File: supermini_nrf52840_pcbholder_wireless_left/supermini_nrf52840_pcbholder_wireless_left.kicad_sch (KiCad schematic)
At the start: 9 parts, among them J1 Conn_01x07_Pin, J2 Conn_01x02_Pin, J3 Conn_01x07_Pin, J4 Conn_01x04_Pin, SW1 SW_SPDT, SW2 SW_SPST, U1 nice_nano

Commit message: create left side and tweaks
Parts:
- removed J1, J3: Conn_01x07_Pin, Connector_PinHeader_2.54mm:PinHeader_1x07_P2.54mm_Vertical, symbol Connector:Conn_01x07_Pin
- removed J2: Conn_01x02_Pin, Connector_JST:JST_PH_S2B-PH-K_1x02_P2.00mm_Horizontal, symbol Connector:Conn_01x02_Pin
- removed J4: Conn_01x04_Pin, Connector_JST:JST_PH_S4B-PH-K_1x04_P2.00mm_Horizontal, symbol Connector:Conn_01x04_Pin
- added J1: Conn_01x02, Connector_JST:JST_PH_S2B-PH-K_1x02_P2.00mm_Horizontal, symbol Connector_Generic:Conn_01x02
- added J2: Conn_01x04, Connector_JST:JST_PH_S4B-PH-K_1x04_P2.00mm_Horizontal, symbol Connector_Generic:Conn_01x04
- added J3, J4: Conn_01x07, Connector_PinHeader_2.54mm:PinHeader_1x07_P2.54mm_Vertical, symbol Connector_Generic:Conn_01x07
- added R1, R2: 4.7k, Resistor_SMD:R_0805_2012Metric, symbol ScottoKeebs:Placeholder_Resistor
- H1, H2: footprint #footprint:M1.4_tapping_Hole_rev2 -> mounting-hole:M1.4_tapping_Hole_JLC
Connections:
- net L_BAT_NEG is gone; now on net GND: U1.14 (GND)
- net L_RST_GND is gone; now on net GND: SW2.2 (B), U1.3 (GND)
- net GND: now reaches U1.4 (GND)
- net GND: now also J1.1 (Pin_1), J2.1 (Pin_1)
- net L_BAT_POS renamed BATT_POS
- net L_COL1 renamed COL1
- net COL1: now also J3.1 (Pin_1)
- net L_COL2 renamed COL2
- net COL2: now also J3.2 (Pin_2)
- net L_COL3 renamed COL3
- net COL3: now also J3.3 (Pin_3)
- net L_COL4 renamed COL4
- net COL4: now also J3.4 (Pin_4)
- net L_COL5 renamed COL5
- net COL5: now also J3.5 (Pin_5)
- net L_COL6 renamed COL6
- net COL6: now also J3.6 (Pin_6)
- net L_COL7 renamed COL7
- net COL7: now also J3.7 (Pin_7)
- net L_OLED_SCL renamed OLED_SCL
- net OLED_SCL: now also J2.3 (Pin_3), R1.2
- net L_OLED_SDA renamed OLED_SDA
- net OLED_SDA: now also J2.4 (Pin_4), R2.2
- net L_OLED_VCC renamed VCC
- net VCC: now also J2.2 (Pin_2), R1.1, R2.1
- net L_ROW1 renamed ROW1
- net ROW1: now also J4.1 (Pin_1)
- net L_ROW2 renamed ROW2
- net ROW2: now also J4.2 (Pin_2)
- net L_ROW3 renamed ROW3
- net ROW3: now also J4.3 (Pin_3)
- net L_ROW4 renamed ROW4
- net ROW4: now also J4.4 (Pin_4)
- net L_ROW5 renamed ROW5
- net ROW5: now also J4.5 (Pin_5)
- net L_ROW6 renamed ROW6
- net ROW6: now also J4.6 (Pin_6)
- net L_ROW7 renamed ROW7
- net ROW7: now also J4.7 (Pin_7)
- net L_RST: no longer names the net of SW2.1 (A), U1.15 (RST)
- net L_SW_POS renamed BATT_SW_POS
- net BATT_SW_POS: now also J1.2 (Pin_2)
- no-connect marks 7 -> 8
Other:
- note added: "populate R1 R2 if OLED lacks pull-ups"
- title: (none) -> Left Dactyl Manuform Wireless Supermini nRF52840 Hub

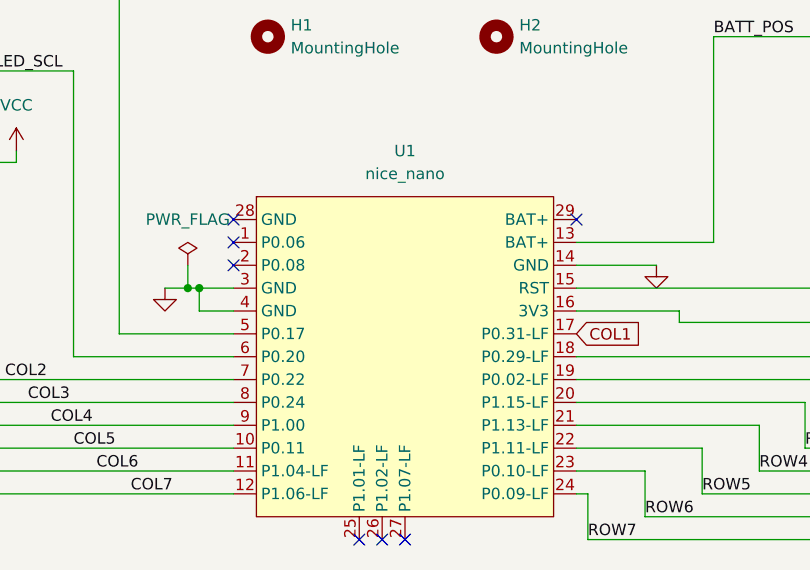
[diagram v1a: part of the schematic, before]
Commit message: remove unused pins from supermini symbol
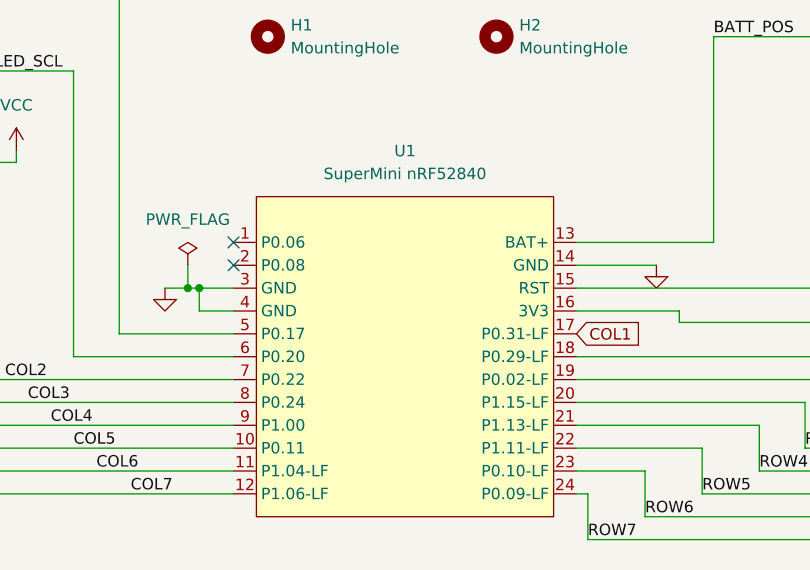
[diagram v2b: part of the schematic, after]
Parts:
- U1: value nice_nano -> SuperMini nRF52840; symbol PCM_marbastlib-promicroish:nice_nano -> Dactyl_SuperMini_Lib:SuperMini_nRF52840_ProMicro
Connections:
- no-connect marks 8 -> 3
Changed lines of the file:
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@@
-	)
-	(no_connect
-		(at 156.21 90.17)
-	)
-	(no_connect
-		(at 134.62 125.73)
 	)
 	(no_connect
@@
 	(no_connect
 		(at 185.42 64.77)
-	)
-	(no_connect
-		(at 137.16 125.73)
-	)
-	(no_connect
-		(at 118.11 90.17)
-	)
-	(no_connect
-		(at 132.08 125.73)
 	)
 	(wire
@@
 	)
 	(symbol
-		(lib_id "PCM_marbastlib-promicroish:nice_nano")
+		(lib_id "Dactyl_SuperMini_Lib:SuperMini_nRF52840_ProMicro")
 		(at 137.16 106.68 0)
 		(unit 1)
@@
 			)
 		)
-		(property "Value" "nice_nano"
+		(property "Value" "SuperMini nRF52840"
 			(at 137.16 85.09 0)
 			(effects
@@
 			)
 		)
-		(property "Datasheet" "https://nicekeyboards.com/docs/nice-nano/pinout-schematic"
+		(property "Datasheet" "https://wiki.icbbuy.com/doku.php?id=developmentboard:nrf52840"
 			(at 138.43 139.7 0)
 			(effects
@@
 			)
 		)
-		(property "Description" "Symbol for an nicekeyboards nice!nano"
+		(property "Description" "Symbol for Supermini nRF52840 with only pro micro compatible pins"
 			(at 137.16 106.68 0)
 			(effects
@@
 		(pin "23"
 		)
-		(pin "25"
-		)
-		(pin "26"
-		)
-		(pin "27"
-		)
-		(pin "28"
-		)
 		(pin "24"
 		)
@@
 		(pin "7"
 		)
-		(pin "29"
-		)
 		(pin "17"
